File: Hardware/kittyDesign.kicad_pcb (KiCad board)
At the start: 2 copper layers, 38.9 x 28.9 mm, 1 part

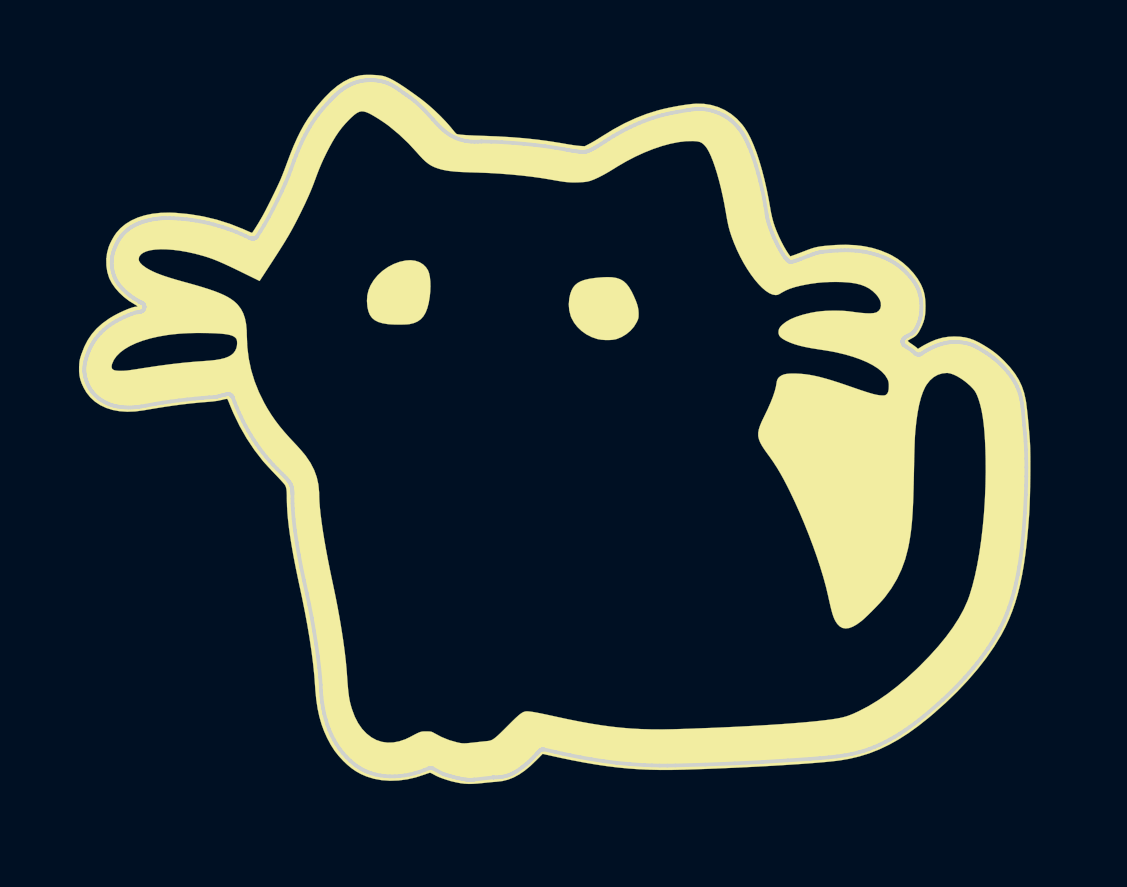
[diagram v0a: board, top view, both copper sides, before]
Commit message: featÑ add routes
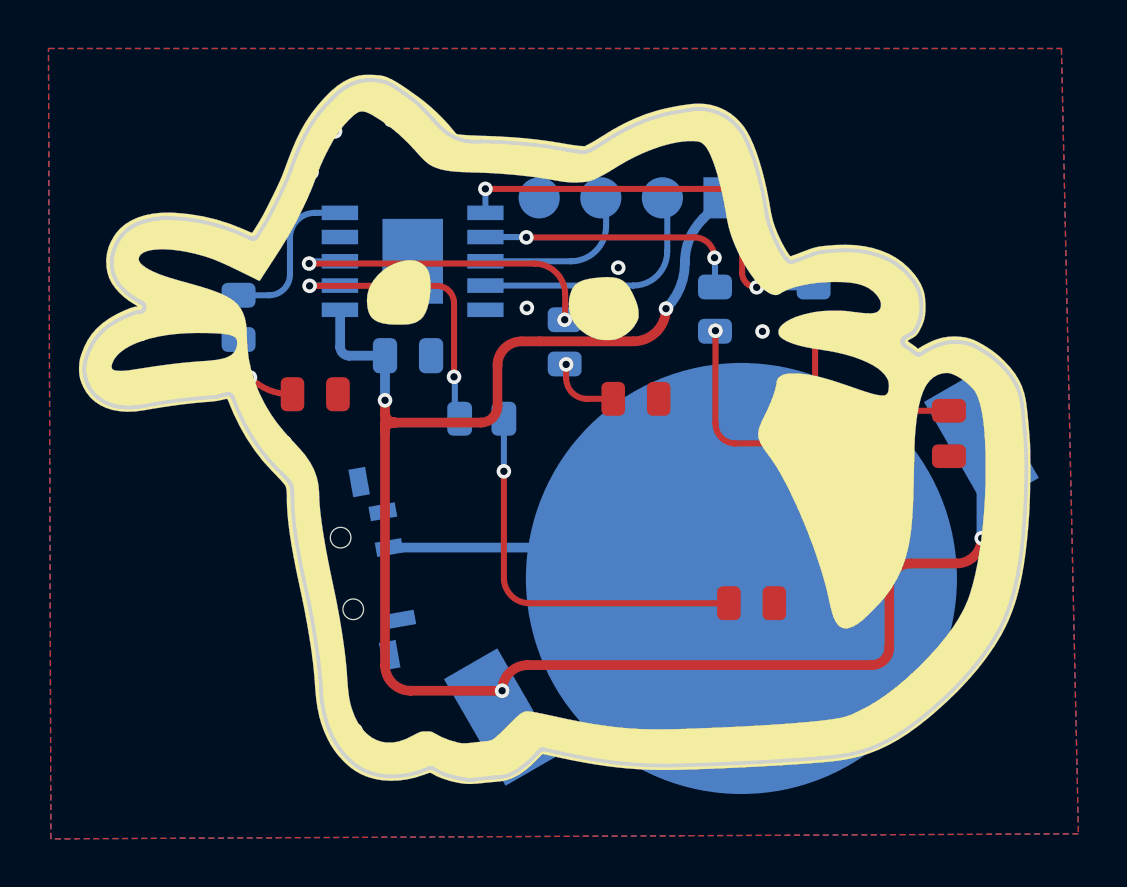
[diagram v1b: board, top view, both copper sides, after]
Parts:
- added BT1: Battery_Cell, footprints:BAT-HLD-001, B.Cu at (121.8, 93.1)
- added C1: 0.1uF, Capacitor_SMD:C_0805_2012Metric, B.Cu at (108.0, 83.9)
- added D1: Blue, LED_SMD:LED_0805_2012Metric, F.Cu at (126.0, 88.5)
- added D2: Green, LED_SMD:LED_0805_2012Metric, F.Cu at (130.3, 87.1)
- added D3: Yellow, LED_SMD:LED_0805_2012Metric, F.Cu at (117.4, 85.7)
- added D4: Red, LED_SMD:LED_0805_2012Metric, F.Cu at (122.2, 94.1)
- added D5: Orange, LED_SMD:LED_0805_2012Metric, F.Cu at (104.2, 85.5)
- added J1: Conn_01x04_Socket, Connector_PinHeader_2.54mm:PinHeader_1x04_P2.54mm_Vertical, B.Cu at (121.0, 77.4)
- added R1: 330R, Resistor_SMD:R_0805_2012Metric, B.Cu at (124.7, 82.0)
- added R2: 330R, Resistor_SMD:R_0805_2012Metric, B.Cu at (114.5, 83.3)
- added R3: 330R, Resistor_SMD:R_0805_2012Metric, B.Cu at (111.0, 86.5)
- added R4: 330R, Resistor_SMD:R_0805_2012Metric, B.Cu at (120.7, 82.0)
- added R5: 330R, Resistor_SMD:R_0805_2012Metric, B.Cu at (101.0, 82.3)
- added SW2: On, footprints:MSK12C02, B.Cu at (105.5, 92.9)
- added U1: PY32F002AA15M6TU, footprints:PY32F002AA15M, B.Cu at (108.2, 80.0)
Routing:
- net +3.3V: track 0.00 -> 72.7 mm, vias 0 -> 4
- net /PA6: track 0.00 -> 17.9 mm, vias 0 -> 2
- net Net-(D4-A): track 0.00 -> 16.4 mm, vias 0 -> 1
- net Net-(BT1--): track 0.00 -> 15.2 mm
- net /PA5: track 0.00 -> 13.6 mm, vias 0 -> 2
- net /PF0: track 0.00 -> 12.5 mm, vias 0 -> 2
- net /PA7: track 0.00 -> 11.1 mm, vias 0 -> 2
- net /SWCLK: track 0.00 -> 10.5 mm
- net Net-(D1-A): track 0.00 -> 9.60 mm, vias 0 -> 1
- net Net-(D2-A): track 0.00 -> 8.49 mm, vias 0 -> 1
- net /SWDIO: track 0.00 -> 7.01 mm
- net /PA1: track 0.00 -> 6.69 mm
- net Net-(D3-A): track 0.00 -> 3.62 mm, vias 0 -> 1
- net Net-(D5-A): track 0.00 -> 3.61 mm, vias 0 -> 1
- net GND: vias 0 -> 24
- added copper zone on B.Cu, net GND
- added copper zone on F.Cu, net GND

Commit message: refactor: change MCU for a ch32v00x
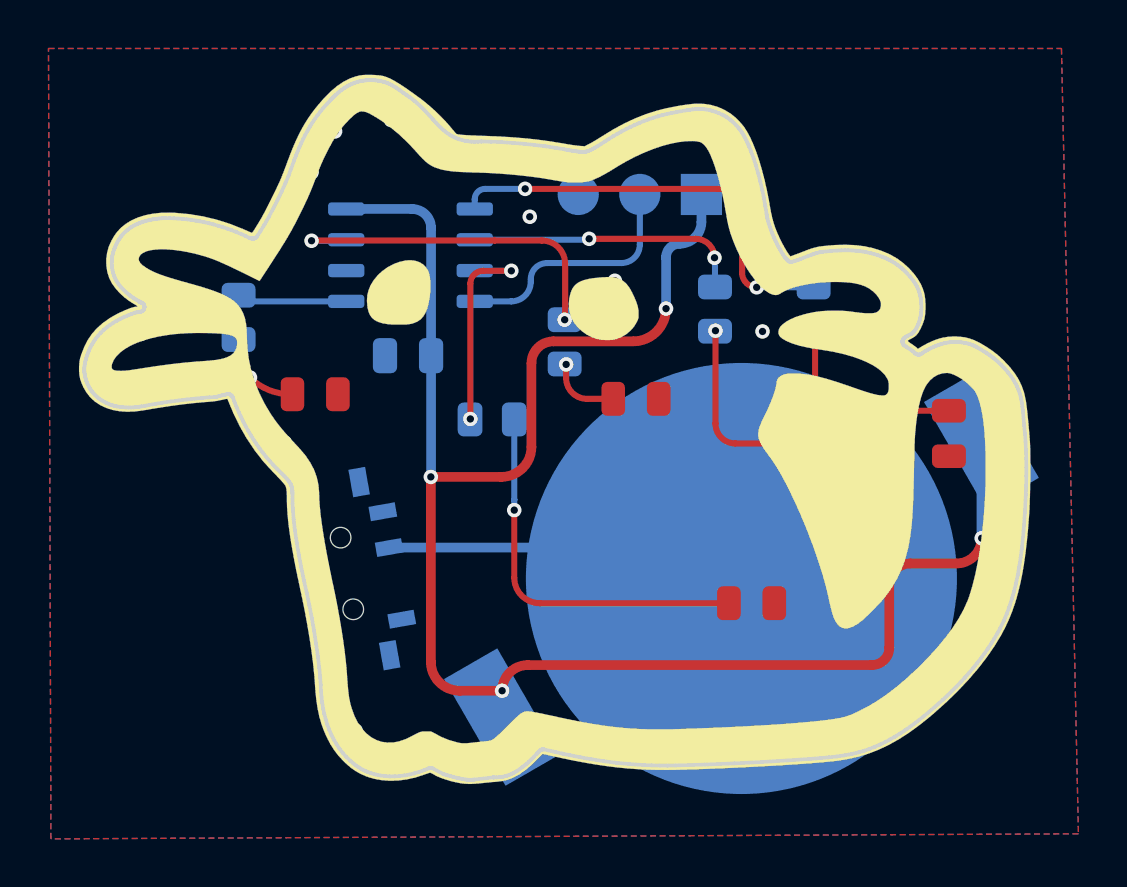
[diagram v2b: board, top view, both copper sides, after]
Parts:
- J1: value Conn_01x04_Socket -> Conn_01x03_Socket; footprint Connector_PinHeader_2.54mm:PinHeader_1x04_P2.54mm_Vertical -> Connector_PinHeader_2.54mm:PinHeader_1x03_P2.54mm_Vertical
- U1: value PY32F002AA15M6TU -> CH32V003JxMx; footprint footprints:PY32F002AA15M -> Package_SO:JEITA_SOIC-8_3.9x4.9mm_P1.27mm
- moved J1 0.94 mm to (120.1, 77.2)
- moved R3 0.43 mm to (111.5, 86.5)
- moved U1 0.27 mm to (108.1, 79.8)
- turned C1 to 180 degrees
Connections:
- net /PA5 renamed /PA2
- J1 pad 2: /SWCLK -> /SWIO
- J1 pad 3: /SWDIO -> GND
- R1 pad 2: /PA6 -> /PC1
- R3 pad 2: /PF0 -> /PC4
- R4 pad 2: /PA7 -> /PC2
- U1 pad 1: +3.3V -> /PA1
- U1 pad 2: /PF0 -> GND
- U1 pad 4: unconnected-(U1-PA0/PF2-NRST-Pad4) -> +3.3V
- U1 pad 5: /PA1 -> /PC1
- U1 pad 6: /PA6 -> /PC2
- U1 pad 7: /PA7 -> /PC4
- U1 pad 8: /SWDIO -> /SWIO
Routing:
- net /PC1: track 0.00 -> 17.9 mm, vias 0 -> 2
- net /PA6: track 17.9 -> 0.00 mm, vias 2 -> 0
- net /PF0: track 12.5 -> 0.00 mm, vias 2 -> 0
- net /PC2: track 0.00 -> 11.5 mm, vias 0 -> 2
- net /PA7: track 11.1 -> 0.00 mm, vias 2 -> 0
- net /SWCLK: track 10.5 -> 0.00 mm
- net /SWIO: track 0.00 -> 10.2 mm
- net /PC4: track 0.00 -> 9.09 mm, vias 0 -> 2
- net /SWDIO: track 7.01 -> 0.00 mm
- net +3.3V: track 72.7 -> 75.4 mm
- net /PA1: track 6.69 -> 4.57 mm
- net /PA2: track 13.6 -> 14.7 mm
- net GND: vias 24 -> 23
